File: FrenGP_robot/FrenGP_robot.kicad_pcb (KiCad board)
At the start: 2 copper layers, 100 x 90 mm, 19 parts, among them J1 Screw_Terminal_01x02, J2 Screw_Terminal_01x02, J3 Screw_Terminal_01x02, SW1 SW_Push

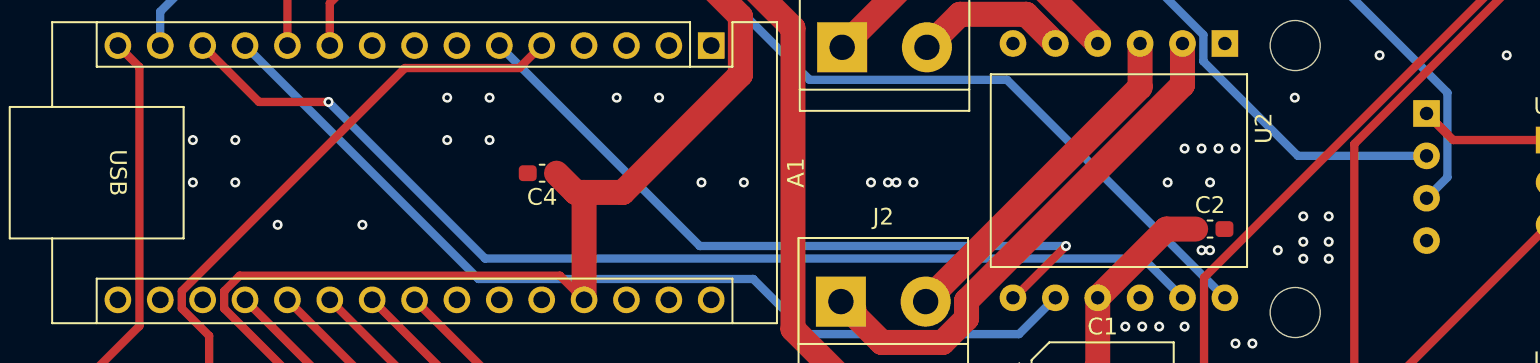
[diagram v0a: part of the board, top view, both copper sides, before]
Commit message: Update to KiCAD 9 Fixed Ultrasonic sensor footprint
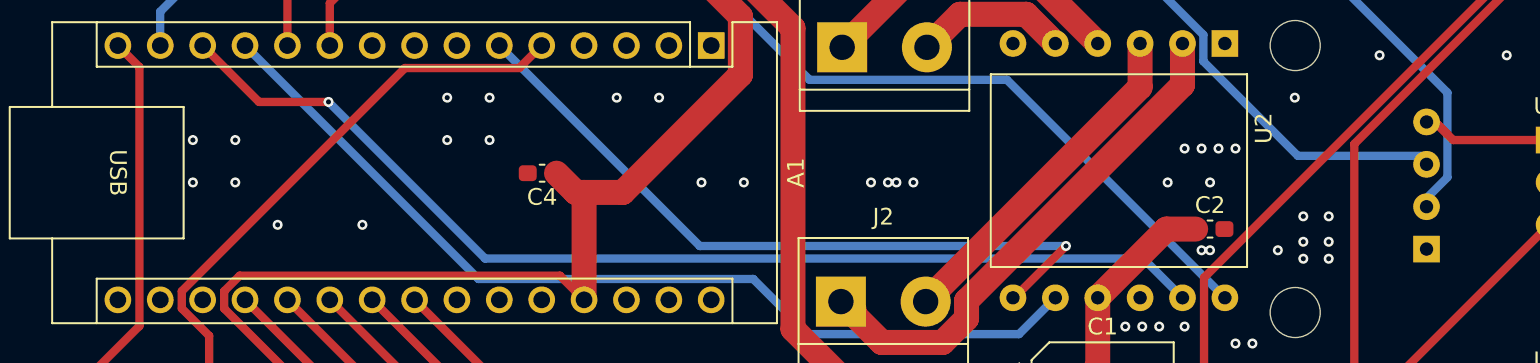
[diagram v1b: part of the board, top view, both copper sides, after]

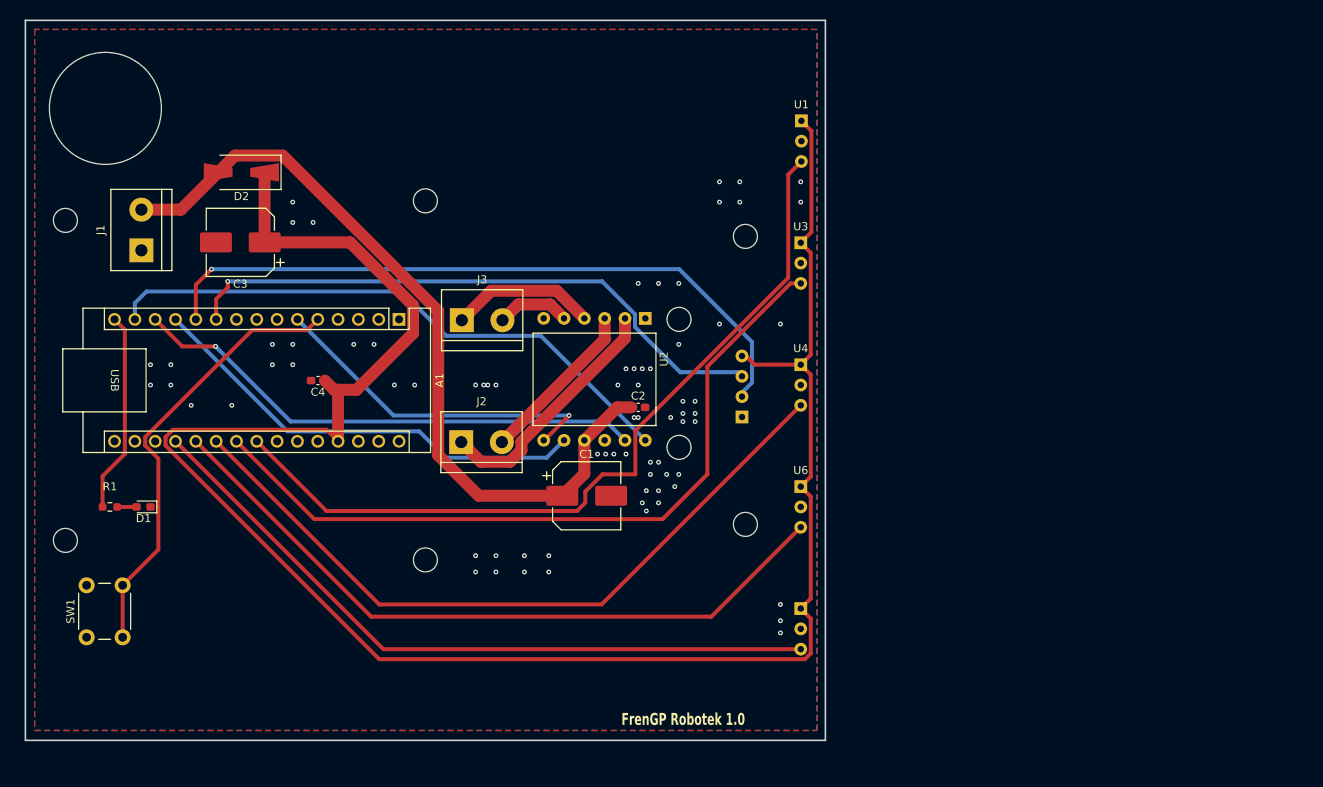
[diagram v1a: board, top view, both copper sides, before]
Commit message: Buzzer HC-05 LED blinkers Second pin rows
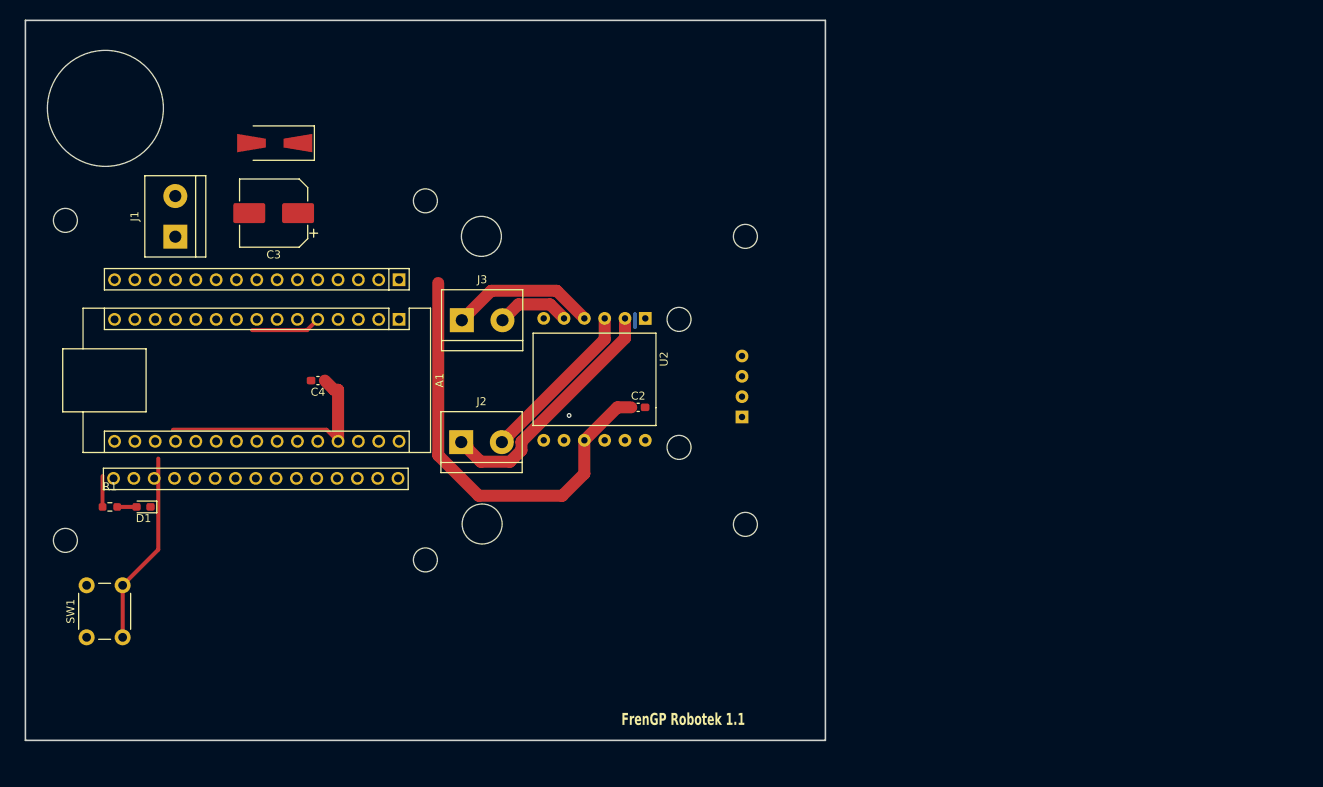
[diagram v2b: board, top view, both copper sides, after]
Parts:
- removed C1: 470u, Capacitor_SMD:CP_Elec_8x6.2
- removed U1, U3, U4, U6, U7: ~, DRV_8833_module:3pin_Reflection_sensor
- moved C3 5.54 mm to (56.0, 47.1)
- moved D2 5.54 mm to (56.2, 38.3)
- moved J1 4.57 mm to (43.7, 50.0)
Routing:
- net +5V_MCU: track 251.6 -> 29.8 mm
- net IR1: track 101.3 -> 0.00 mm
- net IR2: track 94.7 -> 0.00 mm
- net IR3: track 91.8 -> 0.00 mm
- net IR4: track 89.3 -> 0.00 mm
- net IR5: track 88.9 -> 0.00 mm
- net Echo: track 85.3 -> 1.59 mm, vias 1 -> 0
- net Trig: track 75.3 -> 0.00 mm, vias 1 -> 0
- net BIN2: track 74.1 -> 0.00 mm
- net BIN1: track 65.0 -> 0.00 mm, vias 1 -> 0
- net AIN2: track 56.6 -> 0.00 mm
- net +5V_bat: track 99.2 -> 54.8 mm
- net AIN1: track 43.4 -> 0.07 mm
- net Net-(A1-D2): track 55.2 -> 32.9 mm
- net Net-(A1-D12): track 25.1 -> 3.85 mm
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- removed copper zone on B.Cu, net GND
- removed copper zone on F.Cu, net GND
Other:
- outline, holes or cut-outs redrawn
- board text added: "FrenGP Robotek 1.1"
- board text removed: "FrenGP Robotek 1.0"

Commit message: Footprints added
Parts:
- added BZ1: Buzzer, Buzzer_Beeper:Buzzer_TDK_PS1240P02BT_D12.2mm_H6.5mm, F.Cu at (171.8, 42.1)
- added C1: 470u, Capacitor_SMD:CP_Elec_8x6.2, F.Cu at (173.3, 53.9)
- added D3: LED, Diode_SMD:D_0603_1608Metric_Pad1.05x0.95mm_HandSolder, F.Cu at (183.4, 42.4)
- added D4: LED, Diode_SMD:D_0603_1608Metric_Pad1.05x0.95mm_HandSolder, F.Cu at (183.4, 45.0)
- added R2: 330R, Resistor_SMD:R_0603_1608Metric_Pad0.98x0.95mm_HandSolder, F.Cu at (181.3, 50.2)
- added R3: 0R5, Resistor_SMD:R_0805_2012Metric_Pad1.20x1.40mm_HandSolder, F.Cu at (183.6, 36.7)
- added R4: 0R5, Resistor_SMD:R_0805_2012Metric_Pad1.20x1.40mm_HandSolder, F.Cu at (183.6, 39.6)
- added R5: 330R, Resistor_SMD:R_0603_1608Metric_Pad0.98x0.95mm_HandSolder, F.Cu at (181.3, 52.7)
- added R6: 1k, Resistor_SMD:R_0603_1608Metric_Pad0.98x0.95mm_HandSolder, F.Cu at (181.3, 55.2)
- added R7: 2k, Resistor_SMD:R_0603_1608Metric_Pad0.98x0.95mm_HandSolder, F.Cu at (181.3, 57.8)
- added U1: ~, DRV_8833_module:IR sensor header, F.Cu at (158.6, 35.4)
- added U3: ~, DRV_8833_module:HC-05 header, F.Cu at (164.4, 36.0)
- added U4: ~, DRV_8833_module:OLED display header, F.Cu at (151.4, 36.3)
- J2: value Screw_Terminal_01x02 -> Right motor
- J3: value Screw_Terminal_01x02 -> Left motor
- R1: value R -> 330R
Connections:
- A1 pad 1: unconnected-(A1-D1/TX-Pad1) -> Ard_Tx
- A1 pad 15: Net-(A1-D12) -> unconnected-(A1-D12-Pad15)
- A1 pad 19: IR5 -> IR1
- A1 pad 2: unconnected-(A1-D0/RX-Pad2) -> Ard_Rx
- A1 pad 20: IR4 -> IR2
- A1 pad 22: IR2 -> IR4
- A1 pad 23: IR1 -> SDA
- A1 pad 24: unconnected-(A1-A5-Pad24) -> SCL
- A1 pad 25: unconnected-(A1-A6-Pad25) -> IR5
- A1 pad 7: unconnected-(A1-D4-Pad7) -> Buzzer
- A1 pad 8: unconnected-(A1-D5-Pad8) -> Blinker_L
- A1 pad 9: unconnected-(A1-D6-Pad9) -> Blinker_R
- R1 pad 2: Net-(A1-D12) -> Blinker_R
- U2 pad 2: Net-(J2-Pin_1) -> Net-(U2-OUT1)
- U2 pad 4: Net-(J3-Pin_1) -> Net-(U2-OUT3)
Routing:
- net +5V_MCU: track 29.8 -> 8.28 mm
- net Net-(A1-D12): track 3.85 -> 0.00 mm
- net Blinker_R: track 0.00 -> 3.85 mm
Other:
- outline, holes or cut-outs redrawn

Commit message: Rev 1.1 finished
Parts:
- BZ1: footprint Buzzer_Beeper:Buzzer_TDK_PS1240P02BT_D12.2mm_H6.5mm -> Buzzer_Beeper:Buzzer_12x9.5RM7.6
- moved BZ1 132.1 mm to (51.8, 97.2)
- moved R2 130.0 mm to (52.6, 31.6), turned to 180 degrees
- moved D3 125.3 mm to (58.6, 31.6), turned to 180 degrees
- moved R1 98.0 mm to (120.0, 34.0), turned to -90 degrees
- moved D1 97.7 mm to (120.0, 28.0), turned to -90 degrees
- moved R4 90.6 mm to (94.4, 56.0), turned to 180 degrees
- moved U1 90.1 mm to (109.3, 110.8), turned to 180 degrees
- moved D4 89.7 mm to (119.6, 108.0), turned to 90 degrees
- moved R3 82.9 mm to (106.9, 68.2), turned to -90 degrees
- moved R7 81.9 mm to (103.5, 32.0), turned to -90 degrees
- moved R6 80.2 mm to (103.5, 35.8), turned to 90 degrees
- moved C1 78.9 mm to (100.0, 83.4)
- moved R5 78.9 mm to (119.6, 102.0), turned to 90 degrees
- moved U4 65.1 mm to (86.7, 29.0), turned to 90 degrees
- moved U3 55.5 mm to (110.0, 25.0)
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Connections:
- R1 pad 2: Blinker_R -> Blinker_L
- R5 pad 2: Blinker_L -> Blinker_R
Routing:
- net +5V_MCU: track 8.28 -> 212.4 mm
- net +5V_bat: track 54.8 -> 171.2 mm
- net Blinker_R: track 3.85 -> 115.3 mm, vias 0 -> 1
- net Blinker_L: track 0.00 -> 92.6 mm, vias 0 -> 1
- net BIN2: track 0.00 -> 90.7 mm, vias 0 -> 1
- net SDA: track 0.00 -> 87.2 mm, vias 0 -> 2
- net SCL: track 0.00 -> 82.1 mm, vias 0 -> 2
- net IR1: track 0.00 -> 80.9 mm
- net Trig: track 0.00 -> 78.7 mm
- net IR2: track 0.00 -> 77.3 mm
- net Echo: track 1.59 -> 76.2 mm
- net IR3: track 0.00 -> 73.7 mm
- net BIN1: track 0.00 -> 70.3 mm
- net IR4: track 0.00 -> 70.2 mm
- net IR5: track 0.00 -> 66.1 mm
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- added copper zone on B.Cu, net GND
- added copper zone on F.Cu, net GND
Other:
- outline, holes or cut-outs redrawn
- board text added: "+5V_bat"
- board text added: "+5V_bat Gnd"
- board text added: "Gnd IR5 IR4 IR3 IR2 IR1 Vcc"
